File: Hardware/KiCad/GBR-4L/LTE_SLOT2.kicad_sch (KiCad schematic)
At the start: 0 parts

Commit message: Add modem and SIM schematics
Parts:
- added C201, C202, C203, C204: 100nF, Capacitor_SMD:C_0603_1608Metric, symbol Device:C
- added C205, C206: 100uF 6.3V low-ESR, Capacitor_SMD:C_1210_3225Metric, symbol Device:C
- added J201: EM7565 M.2 Key B socket, symbol Connector:Bus_M.2_Socket_B
- added J202: MODEM_CONTROL, Connector_PinHeader_2.54mm:PinHeader_1x08_P2.54mm_Vertical, symbol Connector_Generic:Conn_01x08
- added R201: 10k, Resistor_SMD:R_0603_1608Metric, symbol Device:R
- added R202, R203: 100R, Resistor_SMD:R_0603_1608Metric, symbol Device:R
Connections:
- new net +3V3_M2: C201.1, C202.1, C203.1, C204.1, C205.1, C206.1, J201.2 (3.3V), J201.4 (3.3V), J201.70 (3.3V), J201.72 (3.3V), J201.74 (3.3V), J202.1 (Pin_1), R201.1
- new net GND: C201.2, C202.2, C203.2, C204.2, C205.2, C206.2, J201.11 (GND), J201.27 (GND), J201.3 (GND), J201.33 (GND), J201.39 (GND), J201.45 (GND), J201.5 (GND), J201.51 (GND), J201.57 (GND), J201.71 (GND), J201.73 (GND), J202.2 (Pin_2)
- new net M2_FULL_CARD_POWER_OFF#: J201.6 (~{FULL_CARD_POWER_OFF}), J202.4 (Pin_4), R201.2
- new net M2_PWR_EN: J202.3 (Pin_3)
- new net M2_RESET#: J201.67 (~{RESET}), R202.2
- new net M2_RESET_CTRL#: J202.5 (Pin_5), R202.1
- new net M2_SIM_DETECT: J201.66 (SIM_DETECT), J202.8 (Pin_8)
- new net M2_UIM_CLK: J201.32 (UIM-CLK)
- new net M2_UIM_DATA: J201.34 (UIM-DATA)
- new net M2_UIM_PWR: J201.36 (UIM-PWR)
- new net M2_UIM_RESET: J201.30 (UIM-RESET)
- new net M2_WWAN_LED#: J201.10 (GPIO_9/DAS/~{DSS}/~{LED1}), J202.7 (Pin_7)
- new net M2_W_DISABLE#: J201.8 (~{W_DISABLE1}), R203.2
- new net M2_W_DISABLE_CTRL#: J202.6 (Pin_6), R203.1
- new net USB_M2_D+: J201.7 (USB_D+)
- new net USB_M2_D-: J201.9 (USB_D-)
- no-connect marks 0 -> 40
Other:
- note added: "Do not drive module I/O until at least 100 ms after the start of power-up."
- note added: "EM7565 MODEM SLOT 2 — M.2 KEY B 3042"
- note added: "M.2 socket footprint intentionally remains unassigned until the connector height is frozen."
- note added: "Route USB as 90-ohm differential; keep the pair on continuous ground and away from buck switch nodes."
- note added: "USB 2.0 only. PCIe, USB 3.0, secondary SIM, antenna-control and reserved pins are NC."
- title: (none) -> GBR-4L EM7565 slot 2

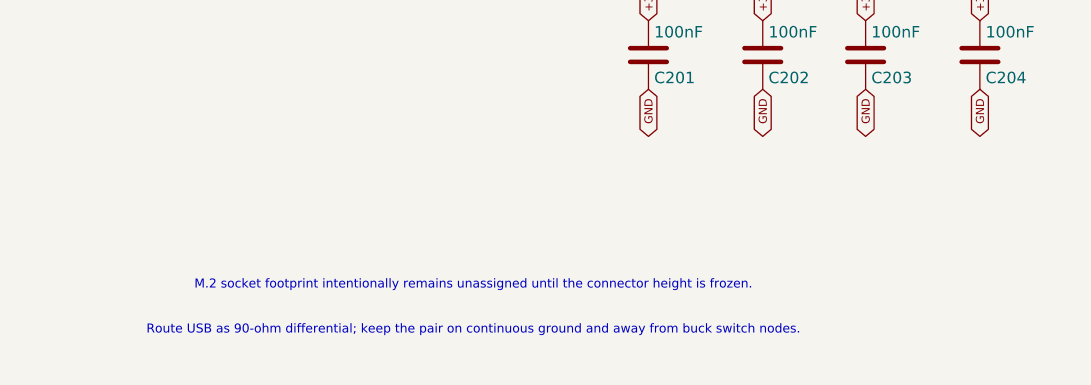
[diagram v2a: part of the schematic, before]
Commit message: Add connector footprints and initial PCB packing
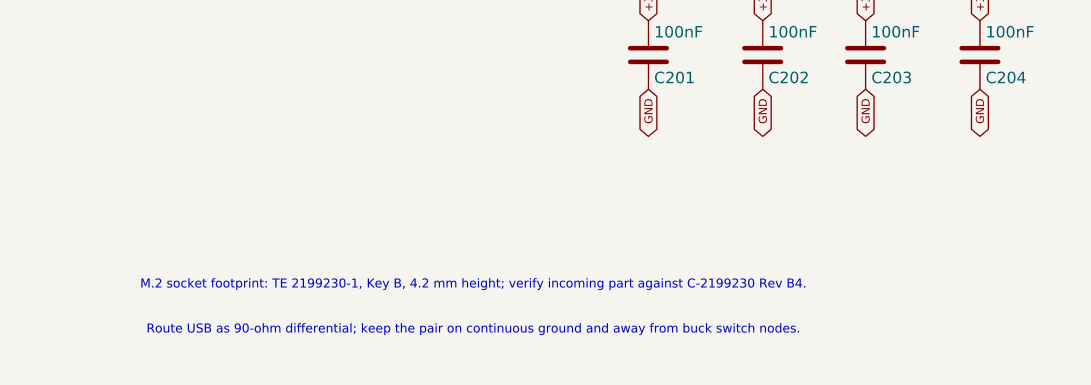
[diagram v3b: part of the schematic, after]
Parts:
- J201: footprint (none) -> GBR-4L:TE_2199230-1_M2_Key-B
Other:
- note added: "M.2 socket footprint: TE 2199230-1, Key B, 4.2 mm height; verify incoming part against C-2199230 Rev B4."
- note removed: "M.2 socket footprint intentionally remains unassigned until the connector height is frozen."
